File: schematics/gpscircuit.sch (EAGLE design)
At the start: 1 part

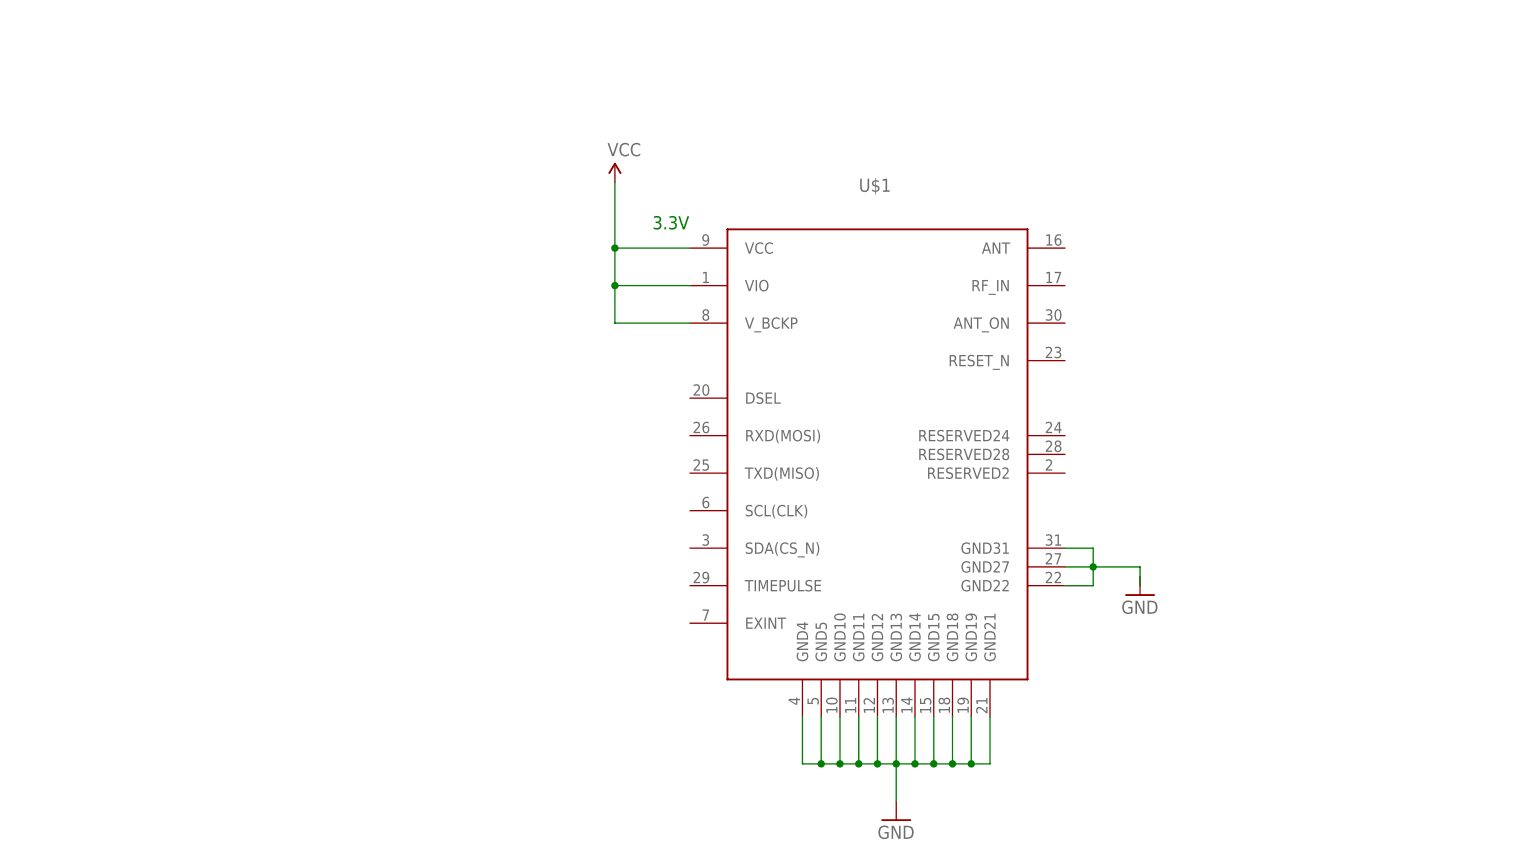
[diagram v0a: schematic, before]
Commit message: Добавлена готовая плата gps (есть мелкие недочеты, которые в ближайшее время будут исправлены)
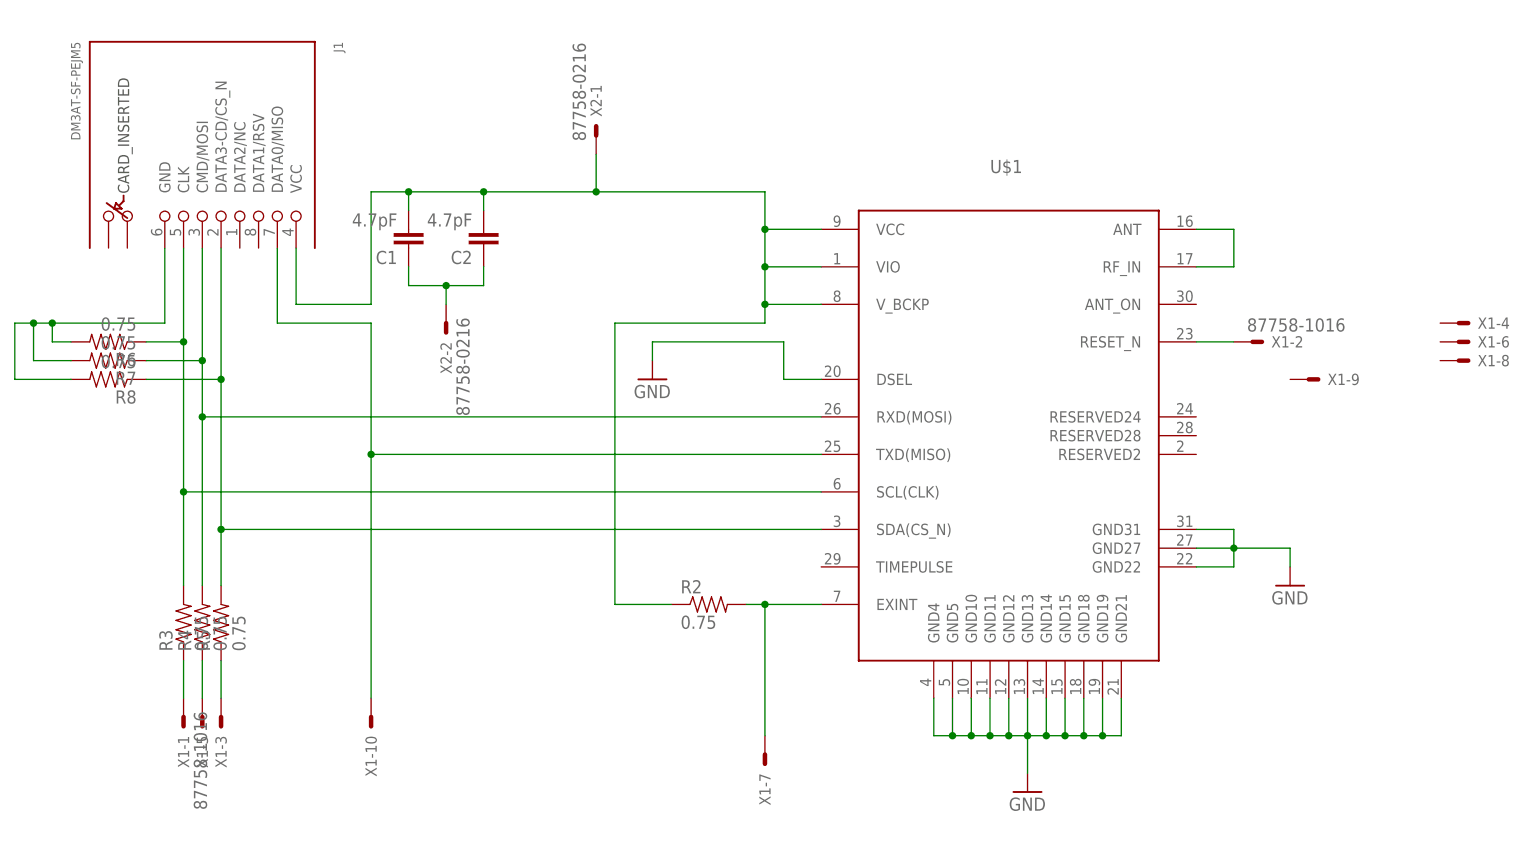
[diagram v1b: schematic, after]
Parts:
- added C1, C2: 4.7pF, SparkFun-Capacitors:4.7PF-50V(-/+.25PF)(0603)
- added J1: DM3AT-SF-PEJM5, connector:DM3AT-SF-PEJM5
- added R2, R3, R4, R5, R6, R7, R8: 0.75, SparkFun-Resistors:0.75OHM-1/4W-1%(0805)
- added X1: 87758-1016, con-molex:87758-1016
- added X2: 87758-0216, con-molex:87758-0216
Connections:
- removed net VCC: U$1.VCC, U$1.VIO, U$1.V_BCKP
- new net 3.3V: C1.2, C2.2, J1.VCC, R2.1, U$1.VCC, U$1.VIO, U$1.V_BCKP, X2-1.S
- new net N$1: U$1.ANT, U$1.RF_IN
- new net N$12: J1.CLK, R3.2, R6.1, U$1.SCL(CLK)
- new net N$14: J1.DATA3-CD/CS_N, R5.2, R8.1, U$1.SDA(CS_N)
- new net N$16: J1.CMD/MOSI, R4.2, R7.1, U$1.RXD(MOSI)
- new net N$3: R2.2, U$1.EXINT
- new net N$4: J1.DATA0/MISO, U$1.TXD(MISO), X1-10.S
- new net N$5: R4.1, X1-5.S
- new net N$6: R5.1, X1-3.S
- new net N$7: J1.GND, R6.2, R7.2, R8.2
- new net N$8: R3.1, X1-1.S
- net GND: now also C1.1, C2.1, U$1.DSEL, U$1.GND22, U$1.GND27, U$1.GND31, X2-2.S
- net N$2: now also U$1.RESET_N, X1-2.S; no longer U$1.GND22, U$1.GND27, U$1.GND31
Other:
- note removed: "3.3V"
- moved on the sheet: U$1

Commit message: Доделала плату gps
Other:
- moved on the sheet: X1-9
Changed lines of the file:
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@@
 <instance part="X1" gate="-7" x="45.72" y="5.08" rot="R270"/>
 <instance part="X1" gate="-8" x="139.7" y="58.42"/>
-<instance part="X1" gate="-9" x="119.38" y="55.88"/>
+<instance part="X1" gate="-9" x="139.7" y="55.88"/>
 <instance part="X1" gate="-10" x="-7.62" y="10.16" rot="R270"/>
 <instance part="X2" gate="-1" x="22.86" y="88.9" rot="R90"/>

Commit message: Немного подраавил разводку (из соображений увеличения антенного полигона)
Немного исправил свойства полигонов (подключение к GND, создание "сиротливых полигонов" и поправил в DRC отступы от края платы

Добавил задание на экспорт гербер файлов на печать плат
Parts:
- removed C2: 4.7pF, SparkFun-Capacitors:4.7PF-50V(-/+.25PF)(0603)
- added C3: (no value), SparkFun-Capacitors:CAP_POL3528
- C1: device SparkFun-Capacitors:4.7PF-50V(-/+.25PF)(0603) -> rcl:C-EUC0603
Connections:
- net 3.3V: now also C3.+; no longer C2.2
- net GND: now also C3.-; no longer C2.1
- net N$3: now also X1-7.S
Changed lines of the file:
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@@
 <part name="GND3" library="SparkFun-Aesthetics" deviceset="GND" device=""/>
 <part name="R2" library="SparkFun-Resistors" deviceset="0.75OHM-1/4W-1%(0805)" device="" value="0.75"/>
-<part name="C1" library="SparkFun-Capacitors" deviceset="4.7PF-50V(-/+.25PF)(0603)" device="" value="4.7pF"/>
-<part name="C2" library="SparkFun-Capacitors" deviceset="4.7PF-50V(-/+.25PF)(0603)" device="" value="4.7pF"/>
+<part name="C1" library="rcl" deviceset="C-EU" device="C0603" value="4.7pF"/>
 <part name="R3" library="SparkFun-Resistors" deviceset="0.75OHM-1/4W-1%(0805)" device="" value="0.75"/>
 <part name="R4" library="SparkFun-Resistors" deviceset="0.75OHM-1/4W-1%(0805)" device="" value="0.75"/>
@@
 <part name="X1" library="con-molex" deviceset="87758-1016" device=""/>
 <part name="X2" library="con-molex" deviceset="87758-0216" device=""/>
+<part name="C3" library="SparkFun-Capacitors" deviceset="CAP_POL" device="3528"/>
+<part name="GND4" library="SparkFun-Aesthetics" deviceset="GND" device=""/>
 </parts>
 <sheets>
@@
 <instance part="GND3" gate="1" x="30.48" y="55.88"/>
 <instance part="R2" gate="G$1" x="38.1" y="25.4"/>
-<instance part="C1" gate="G$1" x="-2.54" y="76.2" rot="R180"/>
-<instance part="C2" gate="G$1" x="7.62" y="76.2" rot="R180"/>
+<instance part="C1" gate="G$1" x="-2.54" y="73.66" rot="R180"/>
 <instance part="R3" gate="G$1" x="-33.02" y="22.86" rot="R90"/>
 <instance part="R4" gate="G$1" x="-30.48" y="22.86" rot="R90"/>
@@
 <instance part="X2" gate="-1" x="22.86" y="88.9" rot="R90"/>
 <instance part="X2" gate="-2" x="2.54" y="63.5" rot="R270"/>
+<instance part="C3" gate="G$1" x="7.62" y="76.2"/>
+<instance part="GND4" gate="1" x="7.62" y="66.04"/>
 </instances>
 <busses>
@@
 <pinref part="C1" gate="G$1" pin="1"/>
 <wire x1="-2.54" y1="71.12" x2="-2.54" y2="68.58" width="0.1524" layer="91"/>
-<pinref part="C2" gate="G$1" pin="1"/>
 <wire x1="-2.54" y1="68.58" x2="2.54" y2="68.58" width="0.1524" layer="91"/>
 <wire x1="2.54" y1="68.58" x2="7.62" y2="68.58" width="0.1524" layer="91"/>
@@
 <junction x="2.54" y="68.58"/>
 <pinref part="X2" gate="-2" pin="S"/>
+<pinref part="C3" gate="G$1" pin="-"/>
+<pinref part="GND4" gate="1" pin="GND"/>
+<junction x="7.62" y="68.58"/>
 </segment>
 </net>
@@
 <pinref part="R2" gate="G$1" pin="2"/>
 <wire x1="53.34" y1="25.4" x2="45.72" y2="25.4" width="0.1524" layer="91"/>
+<pinref part="X1" gate="-7" pin="S"/>
 <wire x1="45.72" y1="25.4" x2="43.18" y2="25.4" width="0.1524" layer="91"/>
-<wire x1="45.72" y1="25.4" x2="45.72" y2="7.62" width="0.1524" layer="91"/>
+<wire x1="45.72" y1="7.62" x2="45.72" y2="25.4" width="0.1524" layer="91"/>
 <junction x="45.72" y="25.4"/>
 </segment>
@@
 <wire x1="33.02" y1="25.4" x2="25.4" y2="25.4" width="0.1524" layer="91"/>
 <wire x1="25.4" y1="25.4" x2="25.4" y2="63.5" width="0.1524" layer="91"/>
-<pinref part="J1" gate="G$1" pin="VCC"/>
-<wire x1="-17.78" y1="73.66" x2="-17.78" y2="66.04" width="0.1524" layer="91"/>
-<wire x1="-17.78" y1="66.04" x2="-7.62" y2="66.04" width="0.1524" layer="91"/>
-<wire x1="-7.62" y1="66.04" x2="-7.62" y2="81.28" width="0.1524" layer="91"/>
-<pinref part="C1" gate="G$1" pin="2"/>
-<wire x1="-7.62" y1="81.28" x2="-2.54" y2="81.28" width="0.1524" layer="91"/>
-<wire x1="-2.54" y1="81.28" x2="-2.54" y2="78.74" width="0.1524" layer="91"/>
-<pinref part="C2" gate="G$1" pin="2"/>
-<wire x1="-2.54" y1="81.28" x2="7.62" y2="81.28" width="0.1524" layer="91"/>
 <wire x1="7.62" y1="81.28" x2="7.62" y2="78.74" width="0.1524" layer="91"/>
-<junction x="-2.54" y="81.28"/>
-<junction x="7.62" y="81.28"/>
 <wire x1="45.72" y1="81.28" x2="22.86" y2="81.28" width="0.1524" layer="91"/>
 <wire x1="22.86" y1="81.28" x2="7.62" y2="81.28" width="0.1524" layer="91"/>
@@
 <junction x="22.86" y="81.28"/>
 <pinref part="X2" gate="-1" pin="S"/>
+<wire x1="-7.62" y1="66.04" x2="-7.62" y2="81.28" width="0.1524" layer="91"/>
+<pinref part="J1" gate="G$1" pin="VCC"/>
+<wire x1="-17.78" y1="73.66" x2="-17.78" y2="66.04" width="0.1524" layer="91"/>
+<wire x1="-17.78" y1="66.04" x2="-7.62" y2="66.04" width="0.1524" layer="91"/>
+<wire x1="-7.62" y1="81.28" x2="-2.54" y2="81.28" width="0.1524" layer="91"/>
+<junction x="7.62" y="81.28"/>
+<pinref part="C1" gate="G$1" pin="2"/>
+<wire x1="-2.54" y1="81.28" x2="7.62" y2="81.28" width="0.1524" layer="91"/>
+<wire x1="-2.54" y1="78.74" x2="-2.54" y2="81.28" width="0.1524" layer="91"/>
+<junction x="-2.54" y="81.28"/>
+<pinref part="C3" gate="G$1" pin="+"/>
 </segment>
 </net>
@@
 </sheet>
 </sheets>
-<errors>
-</errors>
 </schematic>
 </drawing>
